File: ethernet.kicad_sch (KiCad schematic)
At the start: 44 parts, among them IC1 ACPL-217-500E, J6 5-2337992-8, Q17 PJE138K, U22 TPS2372-3RGWR, U23 ULS-12{slash}5-D48N-C

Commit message: PCIE Simplification finished
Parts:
- removed C52: C_100n_0402, jetson-orin-baseboard-footprints:0402-cap, symbol jetson-orin-baseboard:C_100n_0402
- removed C76: C_100n_0805_100V, jetson-orin-baseboard-footprints:0805-cap, symbol jetson-orin-baseboard:C_100n_0805_100V
- removed C79, C80, C81, C82: C_22u_2220_100V, jetson-orin-baseboard-footprints:2220-cap, symbol jetson-orin-baseboard:C_22u_2220_100V
- removed C84, C85: C_47u_16V_1206, jetson-orin-baseboard-footprints:1206-cap, symbol jetson-orin-baseboard:C_47u_16V_1206
- removed D12, D13: CD-MMBL110S, jetson-orin-baseboard-footprints:DFN3538, symbol jetson-orin-baseboard:CD-MMBL110S
- removed D14: PTVS58VS1UR,115, jetson-orin-baseboard-footprints:SOD-123F, symbol jetson-orin-baseboard:PTVS58VS1UR,115
- removed D15: LTST-C190GKT, jetson-orin-baseboard-footprints:LED_0603, symbol jetson-orin-baseboard:LTST-C190GKT
- removed FB2, FB3: BLM21PG221SN1D, jetson-orin-baseboard-footprints:0805-res, symbol jetson-orin-baseboard:BLM21PG221SN1D
- removed IC1: ACPL-217-500E, jetson-orin-baseboard-footprints:SOIC127P700X242-4N, symbol jetson-orin-baseboard:ACPL-217-500E
- removed Q17: PJE138K, jetson-orin-baseboard-footprints:SOT-523, symbol jetson-orin-baseboard:PJE138K
- removed R123: R_1k3_0402, jetson-orin-baseboard-footprints:0402-res, symbol jetson-orin-baseboard:R_1k3_0402
- removed R129, R241: R_0R_0402, jetson-orin-baseboard-footprints:0402-res, symbol jetson-orin-baseboard:R_0R_0402
- removed R142: R_49k9_0402, jetson-orin-baseboard-footprints:0402-res, symbol jetson-orin-baseboard:R_49k9_0402
- removed R145: R_1k2_0402, jetson-orin-baseboard-footprints:0402-res, symbol jetson-orin-baseboard:R_1k2_0402
- removed R146, R154: R_24k9_0402, jetson-orin-baseboard-footprints:0402-res, symbol jetson-orin-baseboard:R_24k9_0402
- removed R148, R149, R150, R153: R_10k_0402, jetson-orin-baseboard-footprints:0402-res, symbol jetson-orin-baseboard:R_10k_0402
- removed R155, R156: R_1k_0402, jetson-orin-baseboard-footprints:0402-res, symbol jetson-orin-baseboard:R_1k_0402
- removed R157, R243: R_0R_0603, jetson-orin-baseboard-footprints:0603-res, symbol jetson-orin-baseboard:R_0R_0603
- removed R185, R229: R_100k_0402, jetson-orin-baseboard-footprints:0402-res, symbol jetson-orin-baseboard:R_100k_0402
- removed R196: R_63R4_0603, jetson-orin-baseboard-footprints:0603-res, symbol jetson-orin-baseboard:R_63R4_0603
- removed R198, R199: R_470k_0402, jetson-orin-baseboard-footprints:0402-res, symbol jetson-orin-baseboard:R_470k_0402
- removed U22: TPS2372-3RGWR, jetson-orin-baseboard-footprints:Texas_RGW0020B, symbol jetson-orin-baseboard:TPS2372-3RGWR
- removed U23: ULS-12/5-D48N-C, jetson-orin-baseboard-footprints:ULS-12_5-D48N-C, symbol jetson-orin-baseboard:ULS-12{brace}slash}5-D48N-C
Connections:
- net PAIR_12: no longer names the net of J6.11 (VC1)
- net PAIR_36: no longer names the net of J6.12 (VC2)
- net PAIR_78: no longer names the net of J6.13 (VC3)
- net PAIR_910: no longer names the net of J6.14 (VC4)
- no-connect marks 2 -> 4
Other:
- note added: "On a pas besoin de PoE dans notre connecteur Ethernet donc voici la recherche digikey pour venir aux nouvelles contraintes. https://www.digikey.ca/en/products/filter/modular-connector-jacks-with-magnetics/365?s=N4IgjCBcoEwBxVAYygMwIYBsDOBTANCAPZQDaIAzAJwDsADDQCwgC6hADgC5QgDKnAJwCWAOwDmIAL6EAbFUQgUkDDgLEyIRmDBxarDt0h9BoidJBw6CpSryESkcozow6FBIWeuKENiC48-MLiUoSuCNCKaFh26o4gMFS6MBT6-obGwWaedACs1tGq9h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"
- note removed: "1/5.7 divider"
- note removed: "Power over Ethernet"
- company: Antmicro Ltd -> Dronolab
- title: Jetson Orin Baseboard -> Ethernet
- moved on the sheet: C77, C78, J6, R147, R151, R152

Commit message: Changed Ethernet Connector
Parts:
- removed J6: 5-2337992-8, jetson-orin-baseboard-footprints:5-2337992-8, symbol jetson-orin-baseboard:5-2337992-8
- added J1: ARJM11C7-502-AB-ER2-T, jetson-orin-baseboard-footprints:ARJM11C7-502-AB-ER2-T, symbol jetson-orin-baseboard:ARJM11C7-502-AB-ER2-T
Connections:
- net +3V3: now also J1.11 (LED_GRN+), J1.13 (LED_YEL+)
- net GBE_MDI0_N: now also J1.2 (P2)
- net GBE_MDI0_P: now also J1.1 (P1)
- net GBE_MDI1_N: now also J1.4 (P4)
- net GBE_MDI1_P: now also J1.3 (P3)
- net GBE_MDI2_N: now also J1.8 (P8)
- net GBE_MDI2_P: now also J1.7 (P7)
- net GBE_MDI3_N: now also J1.10 (P10)
- net GBE_MDI3_P: now also J1.9 (P9)
- net at R152.1: now also J1.12 (LED_GRN-)
- net at R151.1: now also J1.14 (LED_YEL-)
- net at C78.1, R147.2: now also J1.15 (SHIELD1), J1.16 (SHIELD2)
- net at C77.1: now also J1.5 (P5), J1.6 (P6)
- no-connect marks 4 -> 0
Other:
- note removed: "On a pas besoin de PoE dans notre connecteur Ethernet donc voici la recherche digikey pour venir aux nouvelles contraintes. https://www.digikey.ca/en/products/filter/modular-connector-jacks-with-magnetics/365?s=N4IgjCBcoEwBxVAYygMwIYBsDOBTANCAPZQDaIAzAJwDsADDQCwgC6hADgC5QgDKnAJwCWAOwDmIAL6EAbFUQgUkDDgLEyIRmDBxarDt0h9BoidJBw6CpSryESkcozow6FBIWeuKENiC48-MLiUoSuCNCKaFh26o4gMFS6MBT6-obGwWaedACs1tGq9h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"
- moved on the sheet: C77, C78, R147, R151, R152

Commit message: Schematic Done
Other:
- moved on the sheet: C77, C78, R147, R151

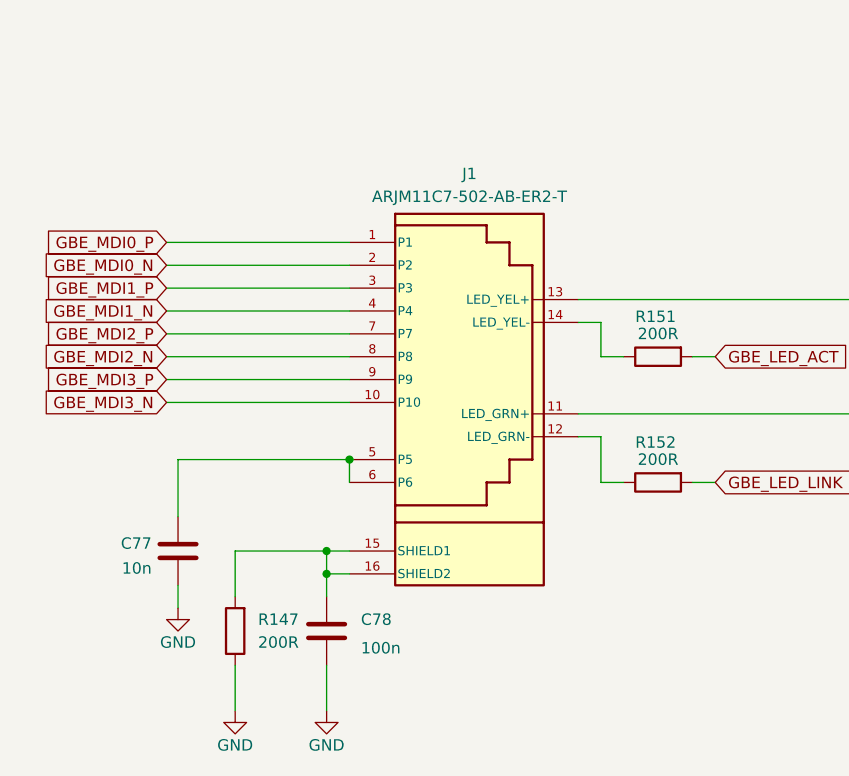
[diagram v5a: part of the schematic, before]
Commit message: Schematic V1 and footprints assigned
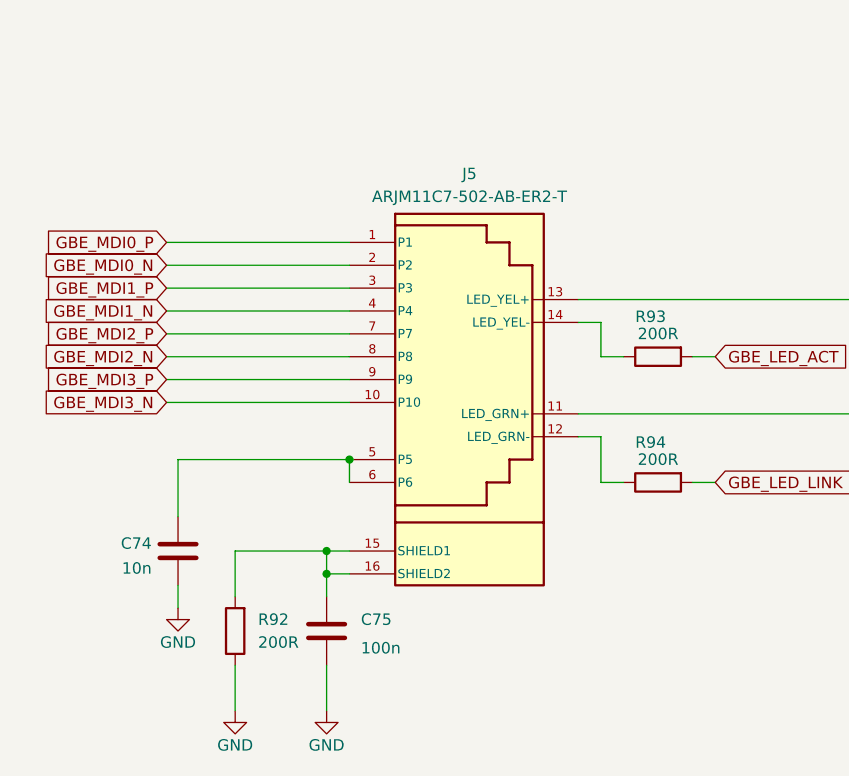
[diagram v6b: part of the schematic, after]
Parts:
- J5: renamed from J1; footprint jetson-orin-baseboard-footprints:ARJM11C7-502-AB-ER2-T -> jetson-orin-baseboard-footprints:ABRACON_ARJM11C7-502-AB-ER2-T
- renumbered C77 to C74, C78 to C75, R147 to R92, R151 to R93, R152 to R94
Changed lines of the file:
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@@
   (symbol (lib_id "jetson-orin-baseboard:GND") (at 166.37 163.83 0) (unit 1)
     (in_bom yes) (on_board yes) (dnp no)
-    (property "Reference" "#PWR0134" (at 166.37 170.18 0)
+    (property "Reference" "#PWR0121" (at 166.37 170.18 0)
       (effects (font (size 1.27 1.27)) hide)
     )
@@
       (project "jetson-orin-baseboard"
         (path "/4b393452-b11e-416e-bc83-918ae3cab2f1/c02b5883-ce9f-434b-a7ad-5c5e18a595c8"
-          (reference "#PWR0134") (unit 1)
+          (reference "#PWR0121") (unit 1)
         )
       )
@@
   (symbol (lib_id "jetson-orin-baseboard:GND") (at 172.72 175.26 0) (unit 1)
     (in_bom yes) (on_board yes) (dnp no) (fields_autoplaced)
-    (property "Reference" "#PWR0135" (at 172.72 181.61 0)
+    (property "Reference" "#PWR0122" (at 172.72 181.61 0)
       (effects (font (size 1.27 1.27)) hide)
     )
@@
       (project "jetson-orin-baseboard"
         (path "/4b393452-b11e-416e-bc83-918ae3cab2f1/c02b5883-ce9f-434b-a7ad-5c5e18a595c8"
-          (reference "#PWR0135") (unit 1)
+          (reference "#PWR0122") (unit 1)
         )
       )
@@
   (symbol (lib_id "jetson-orin-baseboard:+3V3") (at 248.92 125.73 0) (unit 1)
     (in_bom yes) (on_board yes) (dnp no) (fields_autoplaced)
-    (property "Reference" "#PWR0142" (at 248.92 129.54 0)
+    (property "Reference" "#PWR0124" (at 248.92 129.54 0)
       (effects (font (size 1.27 1.27)) hide)
     )
@@
       (project "jetson-orin-baseboard"
         (path "/4b393452-b11e-416e-bc83-918ae3cab2f1/c02b5883-ce9f-434b-a7ad-5c5e18a595c8"
-          (reference "#PWR0142") (unit 1)
+          (reference "#PWR0124") (unit 1)
         )
       )
@@
   (symbol (lib_id "jetson-orin-baseboard:R_200R_0402") (at 219.71 149.86 0) (mirror x) (unit 1)
     (in_bom yes) (on_board yes) (dnp no)
-    (property "Reference" "R152" (at 217.17 145.415 0)
+    (property "Reference" "R94" (at 217.17 145.415 0)
       (effects (font (size 1.27 1.27)) (justify left))
     )
@@
       (project "jetson-orin-baseboard"
         (path "/4b393452-b11e-416e-bc83-918ae3cab2f1/c02b5883-ce9f-434b-a7ad-5c5e18a595c8"
-          (reference "R152") (unit 1)
+          (reference "R94") (unit 1)
         )
       )
@@
   (symbol (lib_id "jetson-orin-baseboard:R_200R_0402") (at 219.71 135.89 0) (mirror x) (unit 1)
     (in_bom yes) (on_board yes) (dnp no)
-    (property "Reference" "R151" (at 217.17 131.445 0)
+    (property "Reference" "R93" (at 217.17 131.445 0)
       (effects (font (size 1.27 1.27)) (justify left))
     )
@@
       (project "jetson-orin-baseboard"
         (path "/4b393452-b11e-416e-bc83-918ae3cab2f1/c02b5883-ce9f-434b-a7ad-5c5e18a595c8"
-          (reference "R151") (unit 1)
+          (reference "R93") (unit 1)
         )
       )
@@
   (symbol (lib_id "jetson-orin-baseboard:GND") (at 182.88 175.26 0) (unit 1)
     (in_bom yes) (on_board yes) (dnp no) (fields_autoplaced)
-    (property "Reference" "#PWR0136" (at 182.88 181.61 0)
+    (property "Reference" "#PWR0123" (at 182.88 181.61 0)
       (effects (font (size 1.27 1.27)) hide)
     )
@@
       (project "jetson-orin-baseboard"
         (path "/4b393452-b11e-416e-bc83-918ae3cab2f1/c02b5883-ce9f-434b-a7ad-5c5e18a595c8"
-          (reference "#PWR0136") (unit 1)
+          (reference "#PWR0123") (unit 1)
         )
       )
@@
   (symbol (lib_id "jetson-orin-baseboard:C_100n_0402") (at 182.88 166.37 0) (unit 1)
     (in_bom yes) (on_board yes) (dnp no) (fields_autoplaced)
-    (property "Reference" "C78" (at 186.69 165.1 0)
+    (property "Reference" "C75" (at 186.69 165.1 0)
       (effects (font (size 1.27 1.27)) (justify left))
     )
@@
       (project "jetson-orin-baseboard"
         (path "/4b393452-b11e-416e-bc83-918ae3cab2f1/c02b5883-ce9f-434b-a7ad-5c5e18a595c8"
-          (reference "C78") (unit 1)
+          (reference "C75") (unit 1)
         )
       )
@@
   (symbol (lib_id "jetson-orin-baseboard:C_10n_0402") (at 166.37 157.48 0) (unit 1)
     (in_bom yes) (on_board yes) (dnp no) (fields_autoplaced)
-    (property "Reference" "C77" (at 163.4491 156.6454 0)
+    (property "Reference" "C74" (at 163.4491 156.6454 0)
       (effects (font (size 1.27 1.27)) (justify right))
     )
@@
       (project "jetson-orin-baseboard"
         (path "/4b393452-b11e-416e-bc83-918ae3cab2f1/c02b5883-ce9f-434b-a7ad-5c5e18a595c8"
-          (reference "C77") (unit 1)
+          (reference "C74") (unit 1)
         )
       )
@@
   (symbol (lib_id "jetson-orin-baseboard:ARJM11C7-502-AB-ER2-T") (at 198.12 139.7 0) (unit 1)
     (in_bom yes) (on_board yes) (dnp no) (fields_autoplaced)
-    (property "Reference" "J1" (at 198.755 115.57 0)
+    (property "Reference" "J5" (at 198.755 115.57 0)
       (effects (font (size 1.27 1.27)))
     )
@@
       (effects (font (size 1.27 1.27)))
     )
-    (property "Footprint" "jetson-orin-baseboard-footprints:ARJM11C7-502-AB-ER2-T" (at 200.025 168.275 0)
+    (property "Footprint" "jetson-orin-baseboard-footprints:ABRACON_ARJM11C7-502-AB-ER2-T" (at 200.025 168.275 0)
       (effects (font (size 1.524 1.524)) hide)
     )
@@
       (project "jetson-orin-baseboard"
         (path "/4b393452-b11e-416e-bc83-918ae3cab2f1/c02b5883-ce9f-434b-a7ad-5c5e18a595c8"
-          (reference "J1") (unit 1)
+          (reference "J5") (unit 1)
         )
       )
@@
   (symbol (lib_id "jetson-orin-baseboard:R_200R_0402") (at 172.72 166.37 90) (unit 1)
     (in_bom yes) (on_board yes) (dnp no)
-    (property "Reference" "R147" (at 175.26 165.1 90)
+    (property "Reference" "R92" (at 175.26 165.1 90)
       (effects (font (size 1.27 1.27)) (justify right))
     )
@@
       (project "jetson-orin-baseboard"
         (path "/4b393452-b11e-416e-bc83-918ae3cab2f1/c02b5883-ce9f-434b-a7ad-5c5e18a595c8"
-          (reference "R147") (unit 1)
-        )
-      )
+          (reference "R92") (unit 1)
+        )
+      )

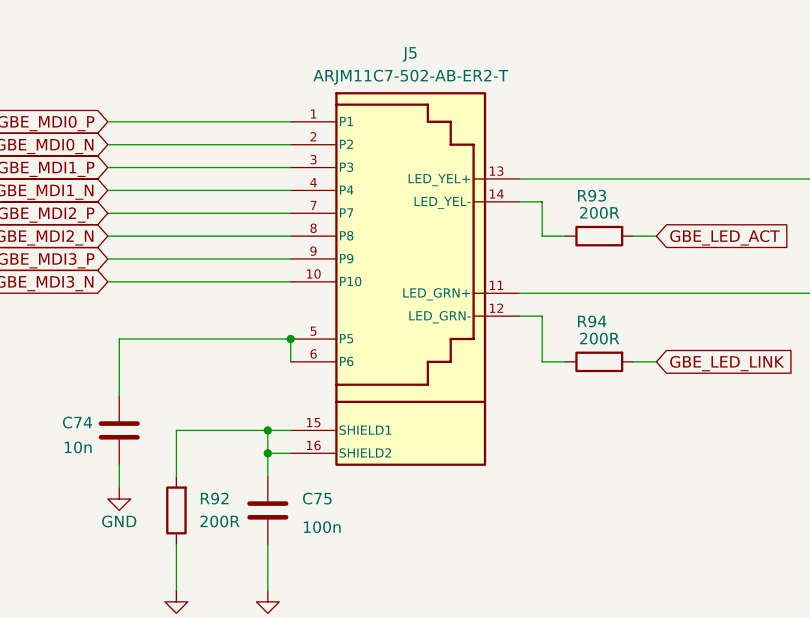
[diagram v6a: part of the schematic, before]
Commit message: Footprints well assigned, XT30 added, Shields grounded
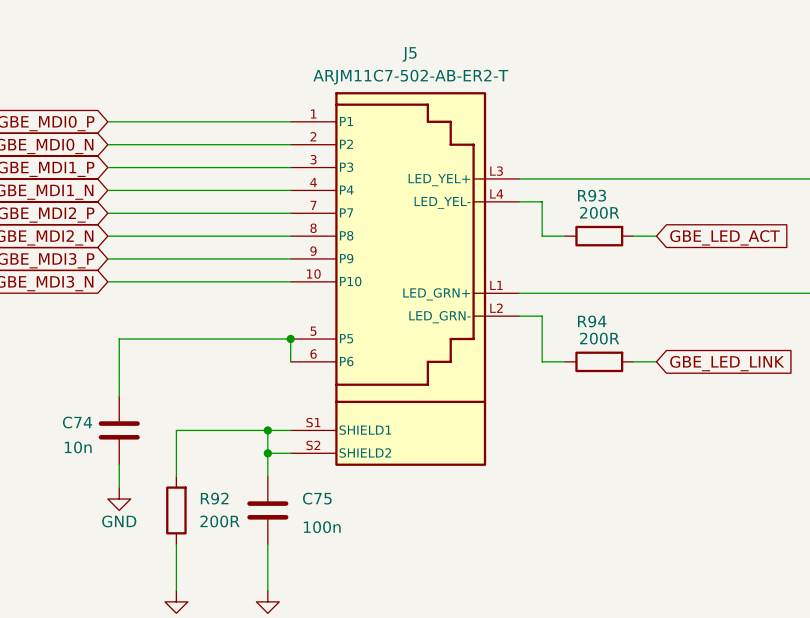
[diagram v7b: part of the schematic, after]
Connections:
- net +3V3: now also J5.L1 (LED_GRN+), J5.L3 (LED_YEL+); no longer J5.11 (LED_GRN+), J5.13 (LED_YEL+)
- net at R94.1: now also J5.L2 (LED_GRN-); no longer J5.12 (LED_GRN-)
- net at R93.1: now also J5.L4 (LED_YEL-); no longer J5.14 (LED_YEL-)
- net at C75.1, R92.2: now also J5.S1 (SHIELD1), J5.S2 (SHIELD2); no longer J5.15 (SHIELD1), J5.16 (SHIELD2)
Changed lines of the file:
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@@
     (pin "1")
     (pin "10")
-    (pin "11")
-    (pin "12")
-    (pin "13")
-    (pin "14")
-    (pin "15")
-    (pin "16")
     (pin "2")
     (pin "3")
@@
     (pin "8")
     (pin "9")
+    (pin "L1")
+    (pin "L2")
+    (pin "L3")
+    (pin "L4")
+    (pin "S1")
+    (pin "S2")
     (instances
       (project "jetson-orin-baseboard"
